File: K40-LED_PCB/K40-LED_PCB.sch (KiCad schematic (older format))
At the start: 29 parts, among them U1 LDD_350HS, U2 LM3466, U3 LM3466, U4 LM3466, U5 LM3466, p1 12V_Pad

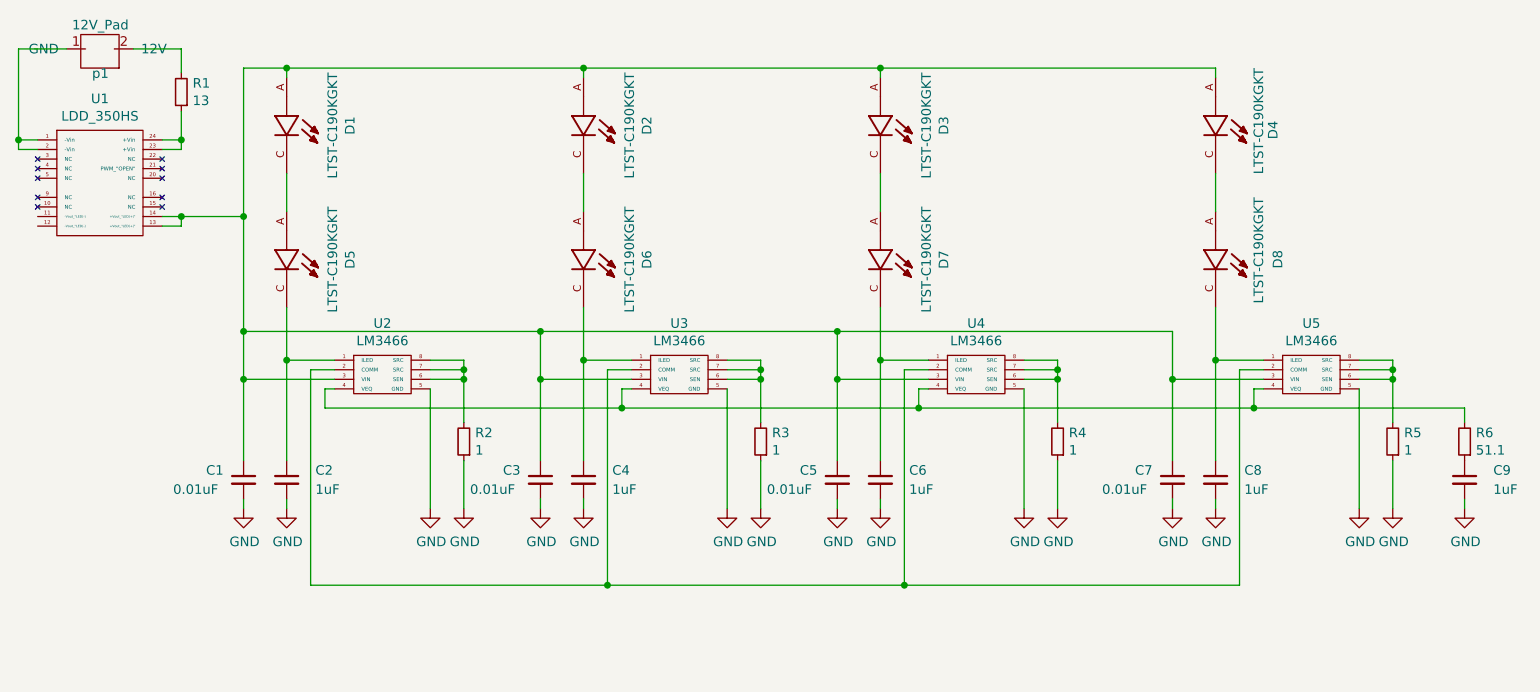
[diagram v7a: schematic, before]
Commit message: PCB  Cathode traces
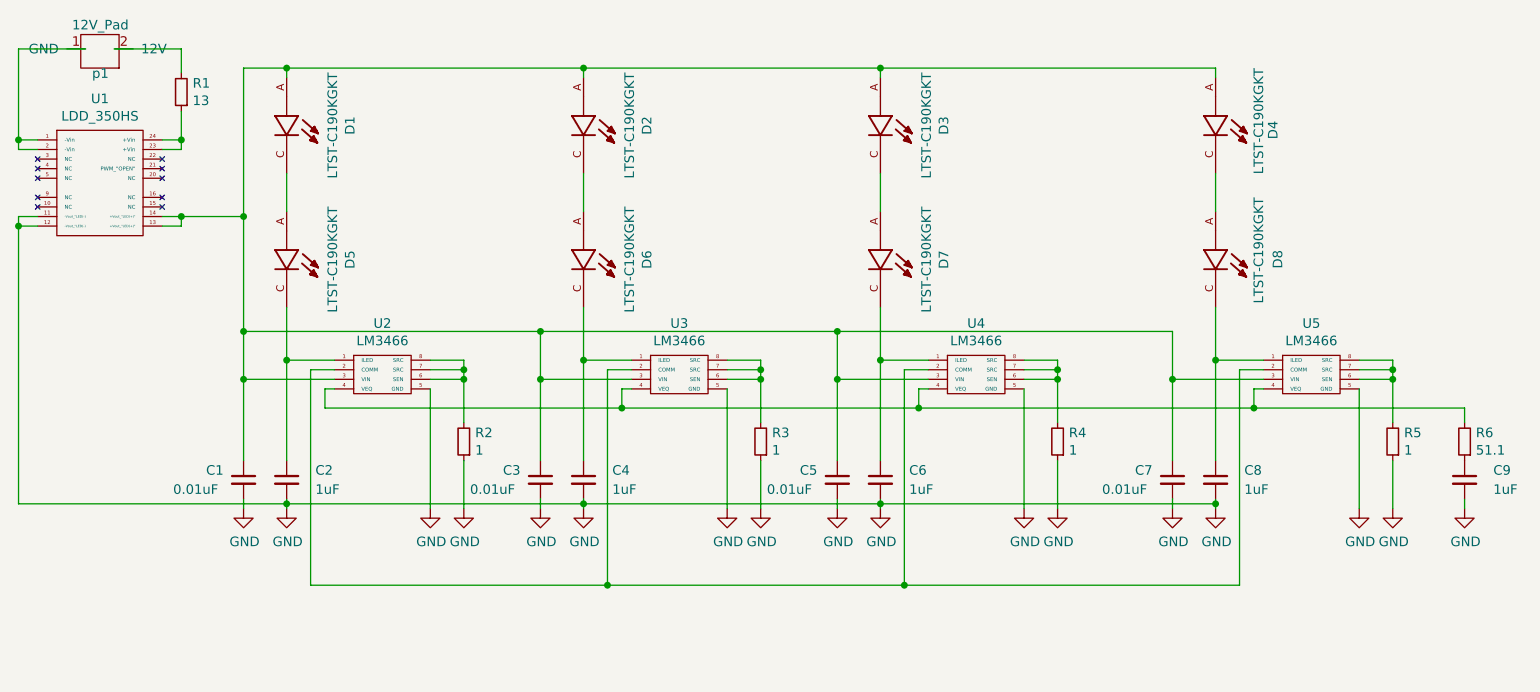
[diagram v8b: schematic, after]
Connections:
- net GND: now also U1.11 (-Vout_"LED(-)), U1.12 (-Vout_"LED(-))
- net at p1.1 (GND): now also U1.1 (-Vin), U1.2 (-Vin)
- net at p1.2 (12V): now also R1.2
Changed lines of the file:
@@
 $EndComp
-Wire Wire Line
-	3950 2350 4200 2350
 Wire Wire Line
 	4200 2825 4100 2825
@@
 Wire Wire Line
 	4200 2875 4100 2875
-Wire Wire Line
-	3600 2350 3350 2350
 Wire Wire Line
 	3350 2350 3350 2825
@@
 	4525 4700 4525 4750
 Wire Wire Line
-	4750 3700 4750 3975
-Wire Wire Line
 	4750 3975 5000 3975
 Wire Wire Line
@@
 $EndComp
 Wire Wire Line
-	4750 4700 4750 4750
+	4750 4700 4750 4725
 Wire Wire Line
 	5675 3975 5675 4025
@@
 	6075 4700 6075 4750
 Wire Wire Line
-	6300 3700 6300 3975
-Wire Wire Line
 	6300 3975 6550 3975
 Wire Wire Line
@@
 $EndComp
 Wire Wire Line
-	6300 4700 6300 4750
+	6300 4700 6300 4725
 Wire Wire Line
 	7225 3975 7225 4025
@@
 $EndComp
 Wire Wire Line
-	7850 4700 7850 4750
+	7850 4700 7850 4725
 Wire Wire Line
 	8775 3975 8775 4025
@@
 	9375 4700 9375 4750
 Wire Wire Line
-	9600 3700 9600 3975
-Wire Wire Line
 	9600 3975 9850 3975
 Wire Wire Line
@@
 	1    0    0    -1
 $EndComp
-Wire Wire Line
-	9600 4700 9600 4750
 Wire Wire Line
 	10525 3975 10525 4025
@@
 	9725 5150 9725 4025
 Wire Wire Line
-	7850 3700 7850 3975
-Wire Wire Line
 	7625 3825 9375 3825
 Connection ~ 7625 3825
@@
 Wire Wire Line
 	10900 4700 10900 4750
+Wire Wire Line
+	3350 2350 3700 2350
+Wire Wire Line
+	3850 2350 4200 2350
+Wire Wire Line
+	3450 3225 3350 3225
+Wire Wire Line
+	3350 3225 3350 3275
+Wire Wire Line
+	3350 3275 3450 3275
+Wire Wire Line
+	9600 3700 9600 3975
+Wire Wire Line
+	7850 3700 7850 3975
+Wire Wire Line
+	6300 3700 6300 3975
+Wire Wire Line
+	4750 3700 4750 3975
+Wire Wire Line
+	3350 3275 3350 4725
+Wire Wire Line
+	3350 4725 4750 4725
+Connection ~ 3350 3275
+Connection ~ 4750 4725
+Wire Wire Line
+	4750 4725 4750 4750
+Wire Wire Line
+	4750 4725 6300 4725
+Connection ~ 6300 4725
+Wire Wire Line
+	6300 4725 6300 4750
+Wire Wire Line
+	6300 4725 7850 4725
+Connection ~ 7850 4725
+Wire Wire Line
+	7850 4725 7850 4750
+Wire Wire Line
+	7850 4725 9600 4725
+Wire Wire Line
+	9600 4700 9600 4725
+Connection ~ 9600 4725
+Wire Wire Line
+	9600 4725 9600 4750
 $EndSCHEMATC
